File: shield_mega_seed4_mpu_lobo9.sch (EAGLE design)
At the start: 39 parts, among them U1 GY-521MPU6050

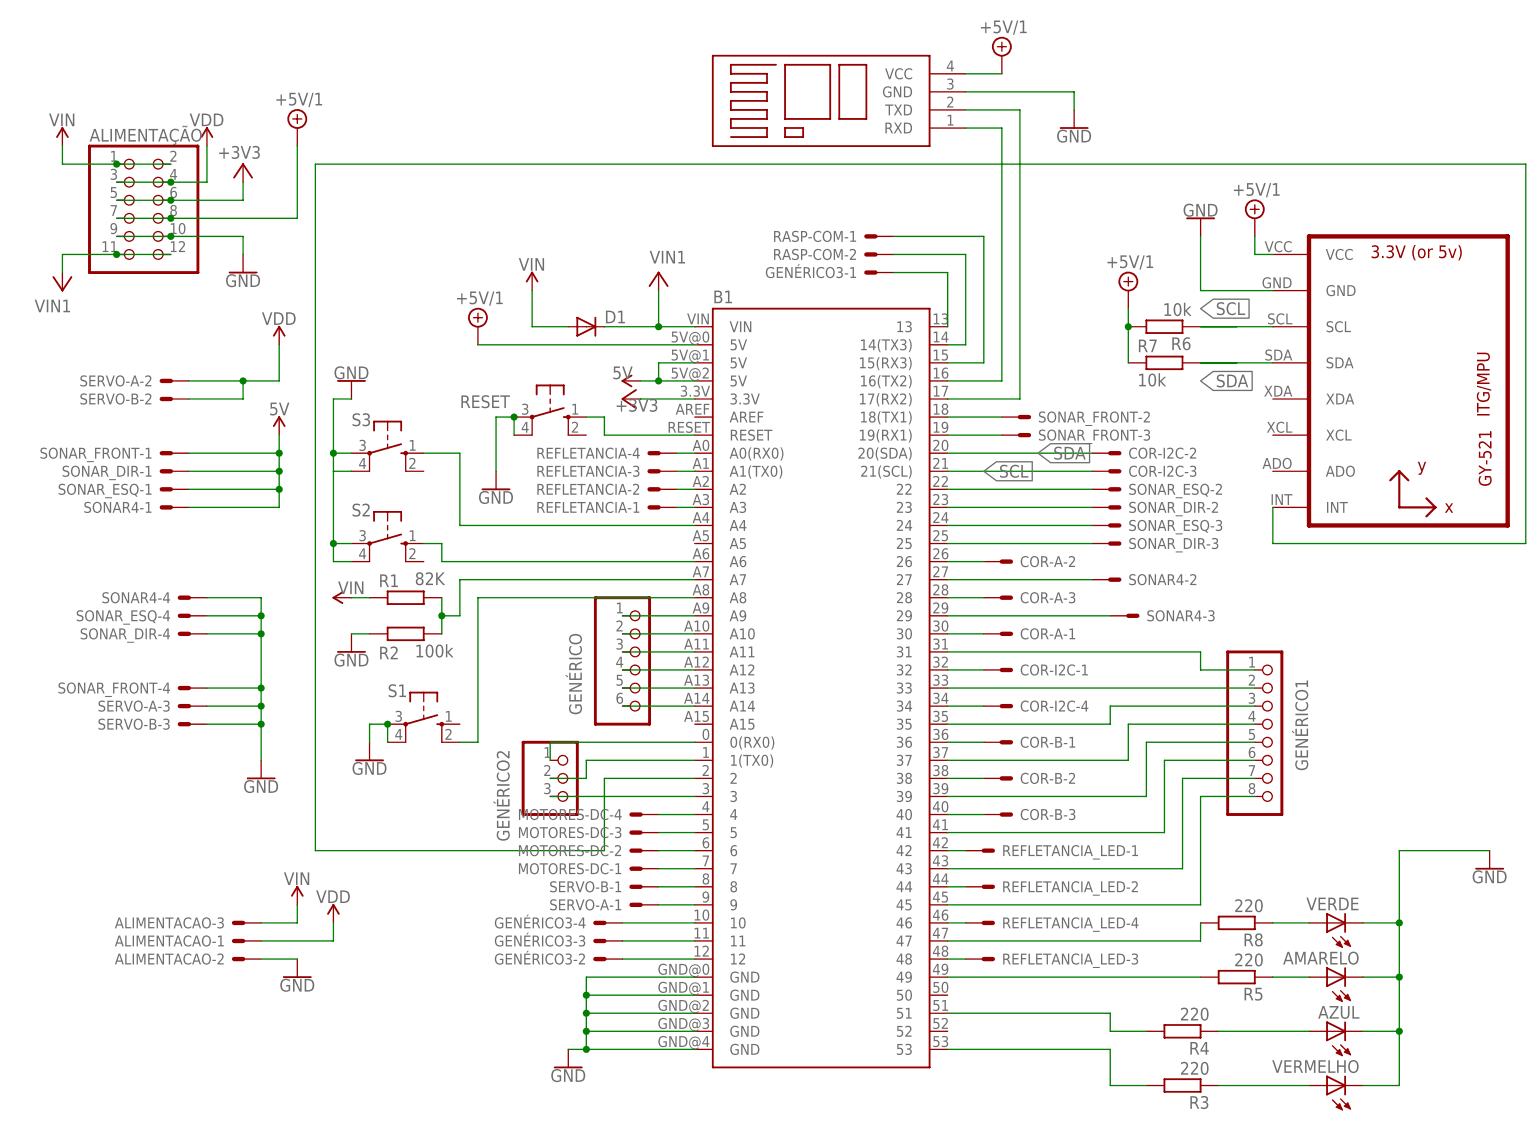
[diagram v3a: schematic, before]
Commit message: Adição de novo layer
Adição de novo layer para os logos
Organização de nomes dos componetes
Pequena modificação do botões para alinha-los
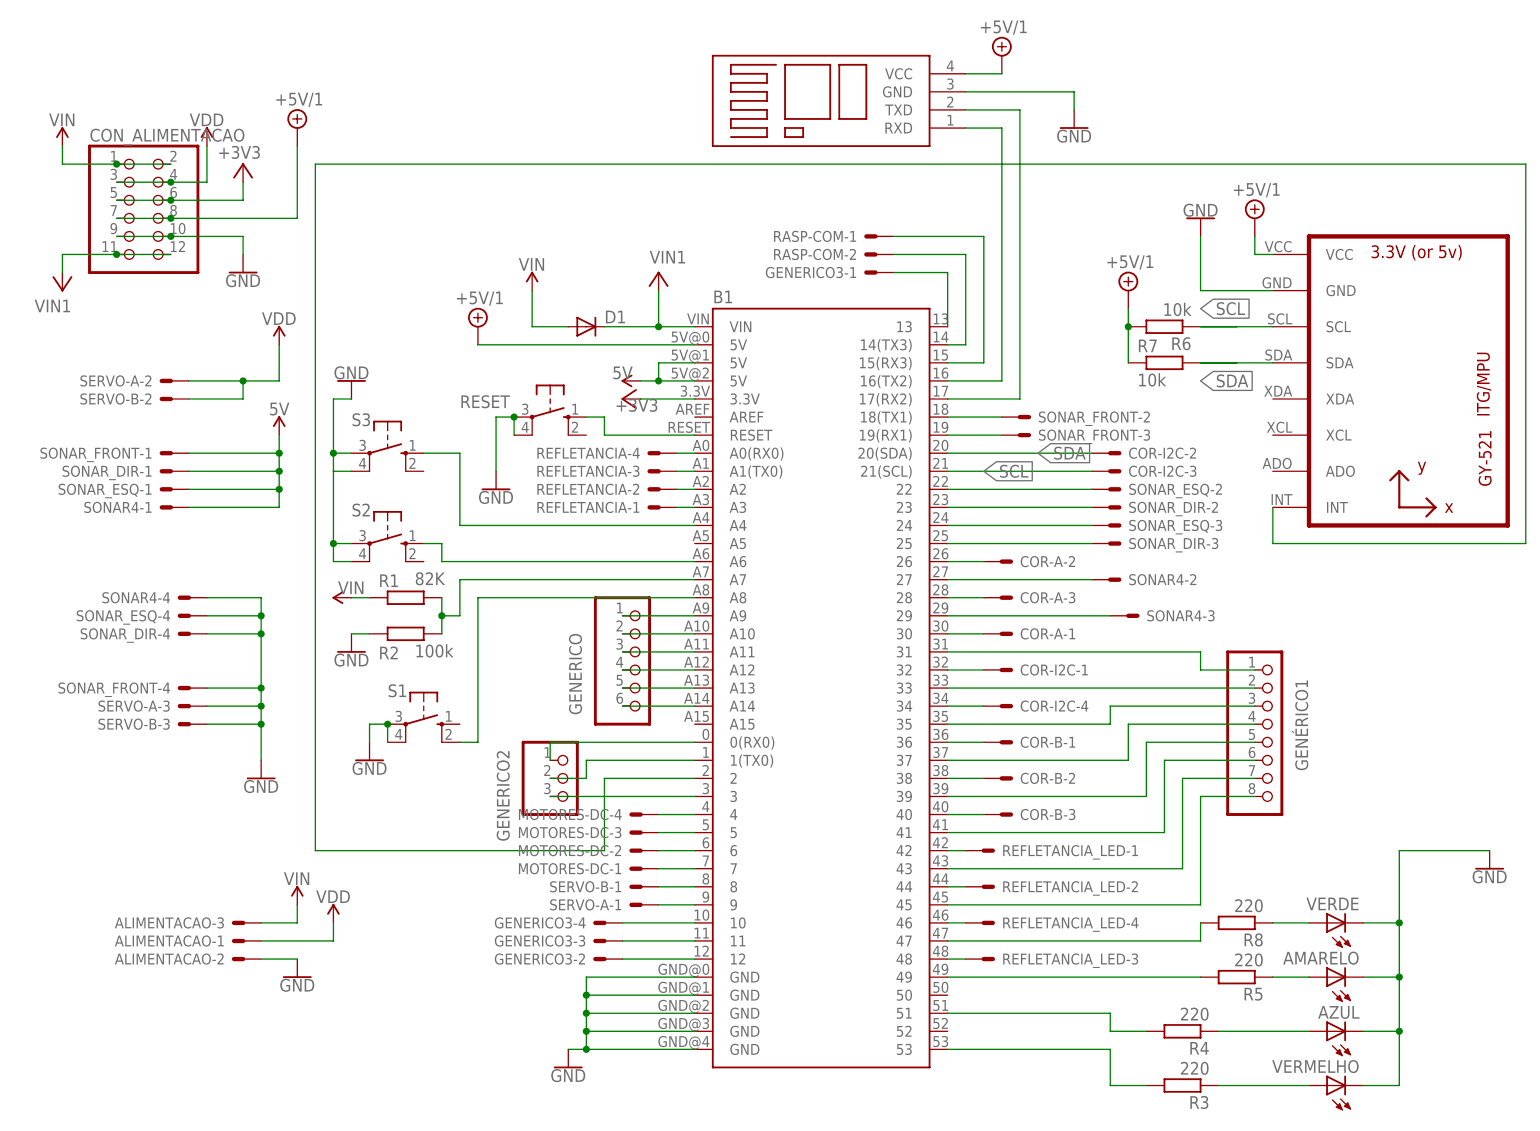
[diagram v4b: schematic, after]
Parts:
- renumbered ALIMENTAÇÃO to CON_ALIMENTACAO, GENÉRICO to GENERICO, GENÉRICO2 to GENERICO2, GENÉRICO3 to GENERICO3
